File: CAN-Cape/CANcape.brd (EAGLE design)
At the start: 58.1 x 77.5 mm, 8 parts

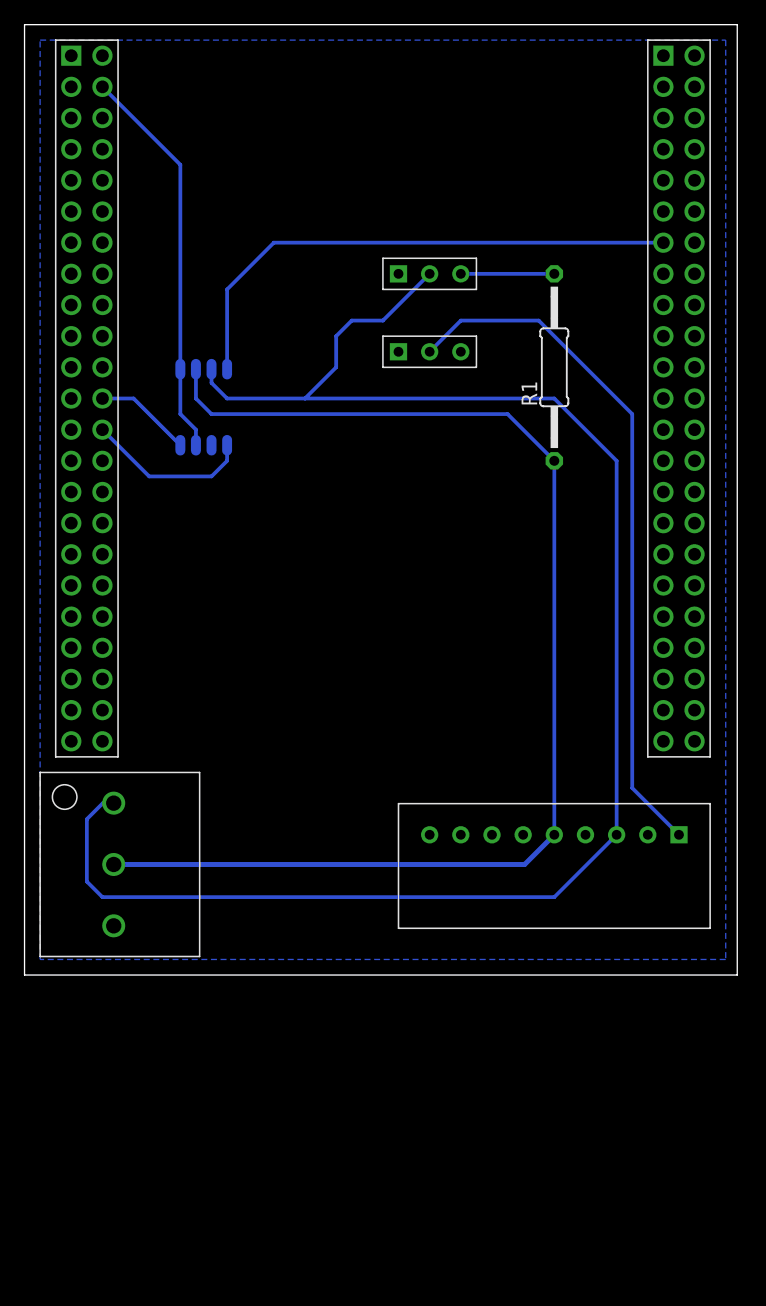
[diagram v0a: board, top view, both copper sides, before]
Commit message: updated board to account for ethernet space conflict
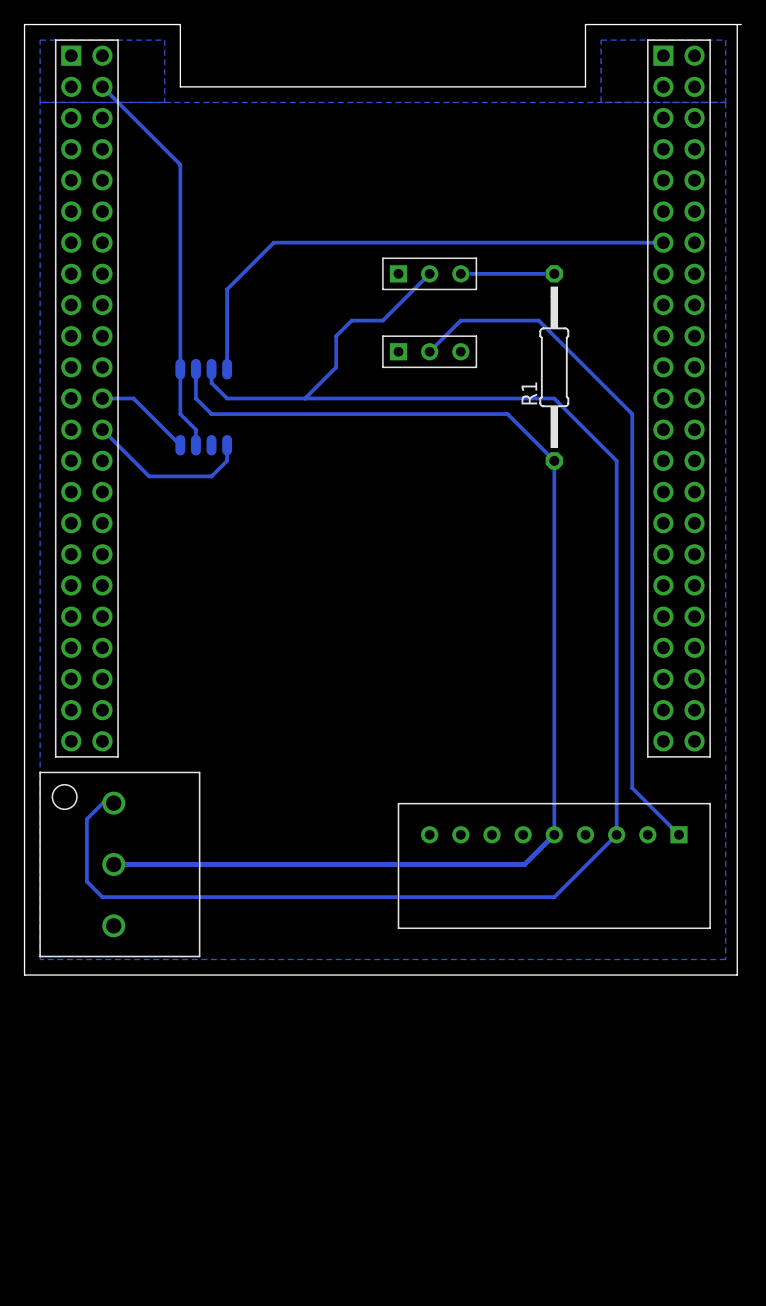
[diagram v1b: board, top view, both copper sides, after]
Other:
- board size 58.1 x 77.5 mm -> 58.4 x 77.5 mm
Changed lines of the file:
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@@
 <wire x1="1.27" y1="-1.27" x2="59.36" y2="-1.27" width="0" layer="20"/>
 <wire x1="59.36" y1="-1.27" x2="59.36" y2="76.19" width="0" layer="20"/>
-<wire x1="59.36" y1="76.19" x2="1.27" y2="76.19" width="0" layer="20"/>
 <wire x1="1.27" y1="76.19" x2="1.27" y2="-1.27" width="0" layer="20"/>
+<wire x1="1.27" y1="76.2" x2="13.97" y2="76.2" width="0" layer="20"/>
+<wire x1="13.97" y1="76.2" x2="13.97" y2="71.12" width="0" layer="20"/>
+<wire x1="13.97" y1="71.12" x2="46.99" y2="71.12" width="0" layer="20"/>
+<wire x1="46.99" y1="71.12" x2="46.99" y2="76.2" width="0" layer="20"/>
+<wire x1="46.99" y1="76.2" x2="59.69" y2="76.2" width="0" layer="20"/>
 </plain>
 <attributes>
@@
 <contactref element="U$7" pad="P$3"/>
 <contactref element="U$5" pad="P$2"/>
-<polygon width="0.3048" layer="16" isolate="0.4064">
-<vertex x="2.54" y="74.93"/>
-<vertex x="58.42" y="74.93"/>
+<polygon width="0" layer="16" isolate="0.3048">
+<vertex x="2.54" y="69.85"/>
+<vertex x="58.42" y="69.85"/>
 <vertex x="58.42" y="0"/>
 <vertex x="2.54" y="0"/>
 </polygon>
-</signal>
+<polygon width="0" layer="16" isolate="0.3048">
+<vertex x="2.54" y="69.85"/>
+<vertex x="2.54" y="74.93"/>
+<vertex x="12.7" y="74.93"/>
+<vertex x="12.7" y="69.85"/>
+</polygon>
+<polygon width="0" layer="16" isolate="0.3048">
+<vertex x="48.26" y="69.85"/>
+<vertex x="48.26" y="74.93"/>
+<vertex x="58.42" y="74.93"/>
+<vertex x="58.42" y="69.85"/>
+</polygon>
+</signal>

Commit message: updated footprints and board design
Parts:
- added U$8: 1X3_HEADER, CANcape:1X3_HEADER
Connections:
- new net 5V: U$1.7, U$1.8, U$8.P$3
- new net TRAN_PWR: U$5.P$3, U$8.P$2
- net 3.3V: now also U$1.3, U$8.P$1; no longer U$5.P$3
- net SGND: now also U$3.P$3
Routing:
- net SGND: track 56.6 -> 105.7 mm
- net 3.3V: track 32.4 -> 80.9 mm
- net TRAN_PWR: track 0.00 -> 46.9 mm
- net 5V: track 0.00 -> 33.3 mm

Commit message: more board work
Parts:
- U$5: value SN65HVD320 -> SOIC_BREAKOUT; device SPST-switch:SN65HVD320 -> CANcape:SOIC_BREAKOUT
- moved U$5 64.1 mm to (8.89, -21.6), flipped to the top
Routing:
- net 3.3V: track 80.9 -> 72.6 mm
- net STANDBY: track 43.6 -> 36.1 mm
- net DCAN1_RX: track 7.93 -> 2.54 mm
- net CANL: track 101.1 -> 98.7 mm
- net TRAN_PWR: track 46.9 -> 44.8 mm
- net CANH: track 136.7 -> 135.6 mm

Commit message: board rev two is ready to go
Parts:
- moved U$5 66.5 mm to (16.5, 44.5), turned to 270 degrees
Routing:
- net 3.3V: track 72.6 -> 87.8 mm
- net STANDBY: track 36.1 -> 49.3 mm
- net CANL: track 98.7 -> 111.0 mm
- net CANH: track 135.6 -> 145.8 mm
- net TRAN_PWR: track 44.8 -> 35.1 mm
- net DCAN1_RX: track 2.54 -> 6.13 mm
- net DCAN1_TX: track 13.5 -> 14.8 mm
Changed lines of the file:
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@@
 <element name="U$7" library="CANcape" package="1X3_HEADER" value="1X3_HEADER" x="34.29" y="49.53"/>
 <element name="U$8" library="CANcape" package="1X3_HEADER" value="1X3_HEADER" x="34.29" y="62.23"/>
-<element name="U$5" library="CANcape" package="SOIC_BREAKOUT" value="SOIC_BREAKOUT" x="8.89" y="-21.59"/>
+<element name="U$5" library="CANcape" package="SOIC_BREAKOUT" value="SOIC_BREAKOUT" x="16.51" y="44.45" rot="R270"/>
 </elements>
 <signals>
 <signal name="DCAN1_RX">
 <contactref element="U$1" pad="24"/>
-<wire x1="10.16" y1="45.72" x2="7.62" y2="45.72" width="0.6096" layer="16"/>
 <contactref element="U$5" pad="P$4"/>
-<wire x1="5.08" y1="-25.4" x2="7.62" y2="45.72" width="0" layer="19" extent="1-1"/>
+<wire x1="7.62" y1="45.72" x2="10.16" y2="45.72" width="0.6096" layer="16"/>
+<wire x1="10.16" y1="45.72" x2="12.7" y2="48.26" width="0.6096" layer="16"/>
 </signal>
 <signal name="DCAN1_TX">
 <contactref element="U$1" pad="26"/>
-<wire x1="7.62" y1="43.18" x2="8.89" y2="43.18" width="0.6096" layer="16"/>
-<wire x1="8.89" y1="43.18" x2="10.16" y2="41.91" width="0.6096" layer="16"/>
-<wire x1="10.16" y1="41.91" x2="10.16" y2="40.64" width="0.6096" layer="16"/>
-<wire x1="10.16" y1="40.64" x2="12.7" y2="38.1" width="0.6096" layer="16"/>
-<wire x1="12.7" y1="38.1" x2="16.51" y2="38.1" width="0.6096" layer="16"/>
-<wire x1="16.51" y1="38.1" x2="17.78" y2="39.37" width="0.6096" layer="16"/>
 <contactref element="U$5" pad="P$1"/>
-<wire x1="5.08" y1="-17.78" x2="12.7" y2="38.1" width="0" layer="19" extent="16-16"/>
+<wire x1="7.62" y1="43.18" x2="10.16" y2="43.18" width="0.6096" layer="16"/>
+<wire x1="10.16" y1="43.18" x2="12.7" y2="45.72" width="0.6096" layer="16"/>
+<wire x1="12.7" y1="45.72" x2="17.78" y2="45.72" width="0.6096" layer="16"/>
+<wire x1="17.78" y1="45.72" x2="20.32" y2="48.26" width="0.6096" layer="16"/>
 </signal>
 <signal name="CANH">
@@
 <wire x1="34.29" y1="55.88" x2="34.29" y2="54.61" width="0.508" layer="16"/>
 <wire x1="34.29" y1="54.61" x2="33.02" y2="53.34" width="0.508" layer="16"/>
-<wire x1="33.02" y1="53.34" x2="30.48" y2="53.34" width="0.508" layer="16"/>
-<wire x1="30.48" y1="53.34" x2="26.67" y2="49.53" width="0.508" layer="16"/>
-<wire x1="26.67" y1="49.53" x2="26.67" y2="48.26" width="0.508" layer="16"/>
-<wire x1="26.67" y1="48.26" x2="24.13" y2="45.72" width="0.508" layer="16"/>
-<wire x1="17.78" y1="45.72" x2="16.51" y2="46.99" width="0.508" layer="16"/>
-<wire x1="49.53" y1="10.16" x2="49.53" y2="40.64" width="0.508" layer="16"/>
-<wire x1="49.53" y1="40.64" x2="44.45" y2="45.72" width="0.508" layer="16"/>
-<wire x1="44.45" y1="45.72" x2="17.78" y2="45.72" width="0.508" layer="16"/>
+<wire x1="33.02" y1="53.34" x2="29.21" y2="53.34" width="0.508" layer="16"/>
+<wire x1="29.21" y1="53.34" x2="26.67" y2="50.8" width="0.508" layer="16"/>
+<wire x1="26.67" y1="50.8" x2="26.67" y2="45.72" width="0.508" layer="16"/>
+<wire x1="46.99" y1="43.18" x2="44.45" y2="45.72" width="0.508" layer="16"/>
+<wire x1="44.45" y1="45.72" x2="26.67" y2="45.72" width="0.508" layer="16"/>
 <wire x1="49.53" y1="10.16" x2="44.45" y2="5.08" width="0.508" layer="16"/>
 <wire x1="8.54" y1="12.74" x2="7.66" y2="12.74" width="0.508" layer="16"/>
@@
 <wire x1="7.62" y1="5.08" x2="44.45" y2="5.08" width="0.508" layer="16"/>
 <contactref element="U$5" pad="P$7"/>
-<wire x1="17.78" y1="45.72" x2="24.13" y2="45.72" width="0" layer="19" extent="16-16"/>
-<wire x1="12.7" y1="-20.32" x2="7.62" y2="5.08" width="0" layer="19" extent="16-16"/>
+<wire x1="26.67" y1="45.72" x2="26.67" y2="38.1" width="0.508" layer="16"/>
+<wire x1="26.67" y1="38.1" x2="24.13" y2="35.56" width="0.508" layer="16"/>
+<wire x1="24.13" y1="35.56" x2="20.32" y2="35.56" width="0.508" layer="16"/>
+<wire x1="20.32" y1="35.56" x2="17.78" y2="38.1" width="0.508" layer="16"/>
+<wire x1="17.78" y1="38.1" x2="17.78" y2="40.64" width="0.508" layer="16"/>
+<wire x1="46.99" y1="43.18" x2="46.99" y2="12.7" width="0.508" layer="16"/>
+<wire x1="46.99" y1="12.7" x2="49.53" y2="10.16" width="0.508" layer="16"/>
 </signal>
 <signal name="CANL">
@@
 <contactref element="U$3" pad="P$2"/>
 <contactref element="U$6" pad="P$5"/>
-<wire x1="15.24" y1="45.72" x2="16.51" y2="44.45" width="0.508" layer="16"/>
-<wire x1="16.51" y1="44.45" x2="40.64" y2="44.45" width="0.508" layer="16"/>
 <wire x1="40.64" y1="44.45" x2="44.45" y2="40.64" width="0.508" layer="16"/>
 <wire x1="8.54" y1="7.74" x2="42.03" y2="7.74" width="0.508" layer="16"/>
@@
 <wire x1="44.45" y1="10.16" x2="44.45" y2="40.64" width="0.508" layer="16"/>
 <contactref element="U$5" pad="P$6"/>
-<wire x1="12.7" y1="-22.86" x2="8.54" y2="7.74" width="0" layer="19" extent="1-1"/>
+<wire x1="40.64" y1="44.45" x2="30.48" y2="44.45" width="0.508" layer="16"/>
+<wire x1="30.48" y1="44.45" x2="29.21" y2="43.18" width="0.508" layer="16"/>
+<wire x1="29.21" y1="43.18" x2="29.21" y2="38.1" width="0.508" layer="16"/>
+<wire x1="29.21" y1="38.1" x2="25.4" y2="34.29" width="0.508" layer="16"/>
+<wire x1="25.4" y1="34.29" x2="16.51" y2="34.29" width="0.508" layer="16"/>
+<wire x1="16.51" y1="34.29" x2="15.24" y2="35.56" width="0.508" layer="16"/>
+<wire x1="15.24" y1="35.56" x2="15.24" y2="40.64" width="0.508" layer="16"/>
 </signal>
 <signal name="GND">
@@
 <contactref element="U$1" pad="2"/>
 <contactref element="U$7" pad="P$3"/>
-<polygon width="0.3048" layer="16" isolate="0.3048">
+<polygon width="0.3048" layer="16" isolate="0.6096">
 <vertex x="1.27" y="76.2"/>
 <vertex x="13.97" y="76.2"/>
@@
 </polygon>
 <contactref element="U$5" pad="P$2"/>
-<wire x1="36.83" y1="49.53" x2="5.08" y2="-20.32" width="0" layer="19" extent="1-1"/>
 </signal>
 <signal name="3.3V">
@@
 <wire x1="33.02" y1="59.69" x2="31.75" y2="60.96" width="0.508" layer="16"/>
 <wire x1="31.75" y1="60.96" x2="31.75" y2="62.23" width="0.508" layer="16"/>
-<wire x1="13.97" y1="57.15" x2="16.51" y2="59.69" width="0.508" layer="16"/>
-<wire x1="16.51" y1="59.69" x2="33.02" y2="59.69" width="0.508" layer="16"/>
+<wire x1="24.13" y1="58.42" x2="25.4" y2="59.69" width="0.508" layer="16"/>
+<wire x1="25.4" y1="59.69" x2="33.02" y2="59.69" width="0.508" layer="16"/>
 <contactref element="U$5" pad="P$5"/>
-<wire x1="12.7" y1="-25.4" x2="13.97" y2="57.15" width="0" layer="19" extent="16-16"/>
+<wire x1="24.13" y1="58.42" x2="24.13" y2="45.72" width="0.508" layer="16"/>
+<wire x1="24.13" y1="45.72" x2="20.32" y2="43.18" width="0.508" layer="16"/>
+<wire x1="20.32" y1="43.18" x2="15.24" y2="43.18" width="0.508" layer="16"/>
+<wire x1="15.24" y1="43.18" x2="12.7" y2="40.64" width="0.508" layer="16"/>
 </signal>
 <signal name="STANDBY">
 <contactref element="U$2" pad="13"/>
-<wire x1="17.78" y1="57.15" x2="19.05" y2="58.42" width="0.508" layer="16"/>
-<wire x1="19.05" y1="58.42" x2="53.34" y2="58.42" width="0.508" layer="16"/>
+<wire x1="25.4" y1="57.15" x2="26.67" y2="58.42" width="0.508" layer="16"/>
+<wire x1="26.67" y1="58.42" x2="53.34" y2="58.42" width="0.508" layer="16"/>
 <contactref element="U$5" pad="P$8"/>
-<wire x1="12.7" y1="-17.78" x2="17.78" y2="57.15" width="0" layer="19" extent="16-16"/>
+<wire x1="25.4" y1="57.15" x2="25.4" y2="41.91" width="0.508" layer="16"/>
+<wire x1="25.4" y1="41.91" x2="24.13" y2="40.64" width="0.508" layer="16"/>
+<wire x1="24.13" y1="40.64" x2="20.32" y2="40.64" width="0.508" layer="16"/>
 </signal>
 <signal name="N$1">
@@
 <wire x1="34.29" y1="49.53" x2="36.83" y2="52.07" width="0.508" layer="16"/>
 <wire x1="36.83" y1="52.07" x2="43.18" y2="52.07" width="0.508" layer="16"/>
-<wire x1="43.18" y1="52.07" x2="50.8" y2="44.45" width="0.508" layer="16"/>
-<wire x1="50.8" y1="44.45" x2="50.8" y2="13.97" width="0.508" layer="16"/>
-<wire x1="50.8" y1="13.97" x2="54.61" y2="10.16" width="0.508" layer="16"/>
+<wire x1="43.18" y1="52.07" x2="49.53" y2="45.72" width="0.508" layer="16"/>
+<wire x1="49.53" y1="45.72" x2="49.53" y2="15.24" width="0.508" layer="16"/>
+<wire x1="49.53" y1="15.24" x2="54.61" y2="10.16" width="0.508" layer="16"/>
 </signal>
 <signal name="TRAN_PWR">
 <contactref element="U$8" pad="P$2"/>
-<wire x1="15.24" y1="43.18" x2="11.43" y2="46.99" width="0.508" layer="16"/>
-<wire x1="11.43" y1="46.99" x2="11.43" y2="60.96" width="0.508" layer="16"/>
-<wire x1="11.43" y1="60.96" x2="15.24" y2="64.77" width="0.508" layer="16"/>
-<wire x1="15.24" y1="64.77" x2="31.75" y2="64.77" width="0.508" layer="16"/>
-<wire x1="31.75" y1="64.77" x2="34.29" y2="62.23" width="0.508" layer="16"/>
 <contactref element="U$5" pad="P$3"/>
-<wire x1="5.08" y1="-22.86" x2="15.24" y2="43.18" width="0" layer="19" extent="16-16"/>
+<wire x1="34.29" y1="62.23" x2="31.75" y2="64.77" width="0.508" layer="16"/>
+<wire x1="31.75" y1="64.77" x2="17.78" y2="64.77" width="0.508" layer="16"/>
+<wire x1="17.78" y1="64.77" x2="15.24" y2="62.23" width="0.508" layer="16"/>
+<wire x1="15.24" y1="62.23" x2="15.24" y2="48.26" width="0.508" layer="16"/>
 </signal>
 <signal name="5V">
